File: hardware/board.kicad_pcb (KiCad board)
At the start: 2 copper layers, 146 x 40 mm, 65 parts, among them IC1 DW01A, J1 Conn_01x03_Male, J2 Conn_01x03_Male, J3 Conn_01x06, J4 Conn_01x06_Female, J5 Conn_01x06, J6 Conn_01x04, J7 Conn_01x02, P1 USB_C_Plug_USB2.0, Q1 AO3400A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

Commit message: PCB routed
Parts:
- added D10: LED, LED_SMD:LED_0805_2012Metric_Pad1.15x1.40mm_HandSolder, F.Cu at (171.2, 82.8)
- added J8: Conn_01x04, Board:Wire-Pad-01x04, B.Cu at (150.5, 90.8)
- added R23: 1k, Resistor_SMD:R_0805_2012Metric_Pad1.20x1.40mm_HandSolder, F.Cu at (171.3, 87.5)
- added R24: 100R, Resistor_SMD:R_0805_2012Metric_Pad1.20x1.40mm_HandSolder, F.Cu at (155.3, 84.9)
- added R25: 1k, Resistor_SMD:R_0805_2012Metric_Pad1.20x1.40mm_HandSolder, F.Cu at (155.2, 82.0)
- added R26: 1k, Resistor_SMD:R_0805_2012Metric_Pad1.20x1.40mm_HandSolder, F.Cu at (155.3, 87.8)
- SW3: footprint Button_Switch_SMD:SW_SPDT_PCM12 -> Board:SW_SPDT_PCM12
- moved C1 12.9 mm to (166.4, 87.7), turned to 180 degrees
- moved J4 12.5 mm to (171.0, 67.2)
- moved U1 11.3 mm to (166.4, 83.5), turned to 90 degrees
- moved C2 6.57 mm to (160.5, 87.7), turned to 180 degrees
- moved C7 5.58 mm to (170.0, 87.6), turned to 0 degrees
- moved IC1 4.69 mm to (170.0, 83.5), turned to 180 degrees
- moved D4 4.00 mm to (211.0, 80.0)
- moved D5 4.00 mm to (203.5, 77.0)
- moved J2 4.00 mm to (216.0, 74.5)
- moved Q2 4.00 mm to (211.0, 79.0)
- moved R5 4.00 mm to (211.0, 77.5)
- moved R6 4.00 mm to (207.5, 79.0)
- moved R7 4.00 mm to (207.5, 74.5)
- moved TP3 4.00 mm to (209.9, 77.0)
- moved TP4 4.00 mm to (212.5, 77.0)
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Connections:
- net /Sheet623EC3BA/AD0 renamed Net-(R10-Pad1)
- net /Sheet623EC3BA/INT renamed Net-(R12-Pad2)
- J5 pad 2: /IO34 -> /IO27
- J5 pad 3: /IO33 -> /IO26
- J5 pad 4: /IO32 -> /IO25
- J5 pad 5: /IO27 -> /IO23
- U3 pad 10: (no net) -> /IO25
- U3 pad 11: (no net) -> /IO26
- U3 pad 37: (no net) -> /IO23
- U3 pad 6: /IO34 -> /LED_B
- U3 pad 8: /IO32 -> /LED_R
- U3 pad 9: /IO33 -> /LED_G
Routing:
- net +5V: track 0.00 -> 165.1 mm
- net GND: track 0.00 -> 162.4 mm, vias 0 -> 12
- net +3V3: track 0.00 -> 150.3 mm, vias 0 -> 8
- net /SCL: track 0.00 -> 104.2 mm, vias 0 -> 1
- net /Sheet6241753E/BATT+_OUT: track 0.00 -> 102.7 mm
- net /LED_A: track 0.00 -> 96.6 mm, vias 0 -> 1
- net /LED_B: track 0.00 -> 95.2 mm, vias 0 -> 2
- net /Sheet6241753E/BATT-: track 0.00 -> 85.2 mm, vias 0 -> 1
- net /SERVO_B: track 0.00 -> 83.7 mm, vias 0 -> 1
- net /Sheet6241753E/BATT+: track 0.00 -> 79.2 mm, vias 0 -> 2
- net /SERVO_A: track 0.00 -> 69.2 mm
- net /IO0: track 0.00 -> 62.3 mm, vias 0 -> 2
- net /MOTOR_A: track 0.00 -> 58.3 mm
- net /Sheet6241753E/VBUS: track 0.00 -> 53.3 mm, vias 0 -> 4
- net /SDA: track 0.00 -> 51.6 mm, vias 0 -> 1
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- added copper zone on B.Cu, net GND
- added copper zone on F.Cu, net GND
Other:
- board size 146 x 40 mm -> 150 x 40 mm
- net class Default: clearance 0.2 -> 0.15; via_dia 0.8 -> 0.6
- rule trace_clearance: 0.2 -> 0.15

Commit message: PCB: Mounting holes for landing gear
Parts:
- added H1: MountingHole, MountingHole:MountingHole_2.2mm_M2, F.Cu at (120.0, 77.0)
- added H2: MountingHole, MountingHole:MountingHole_2.2mm_M2, F.Cu at (198.0, 77.0)

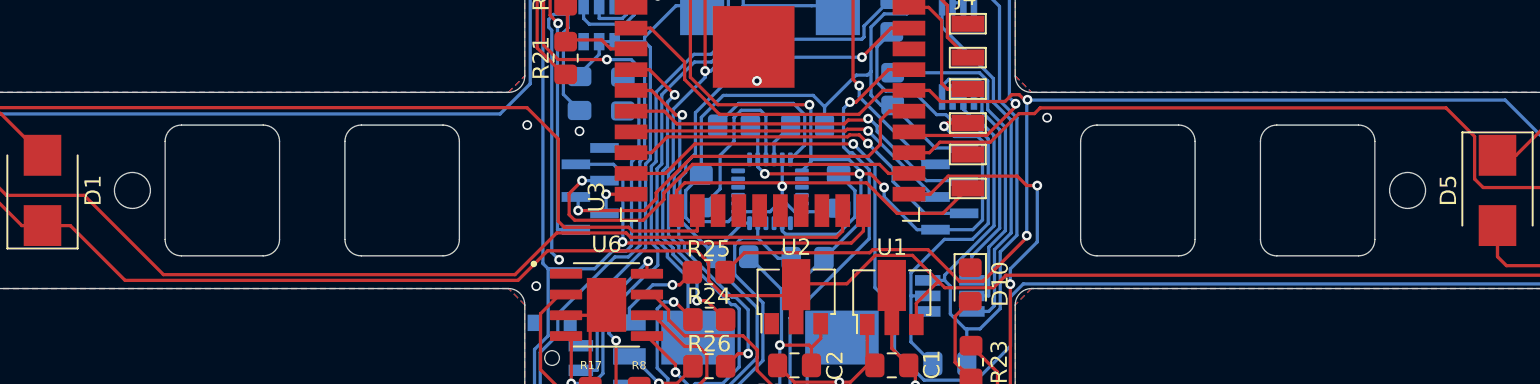
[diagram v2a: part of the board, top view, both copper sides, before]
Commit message: PCB: Holes for LiPo battery zip tie added
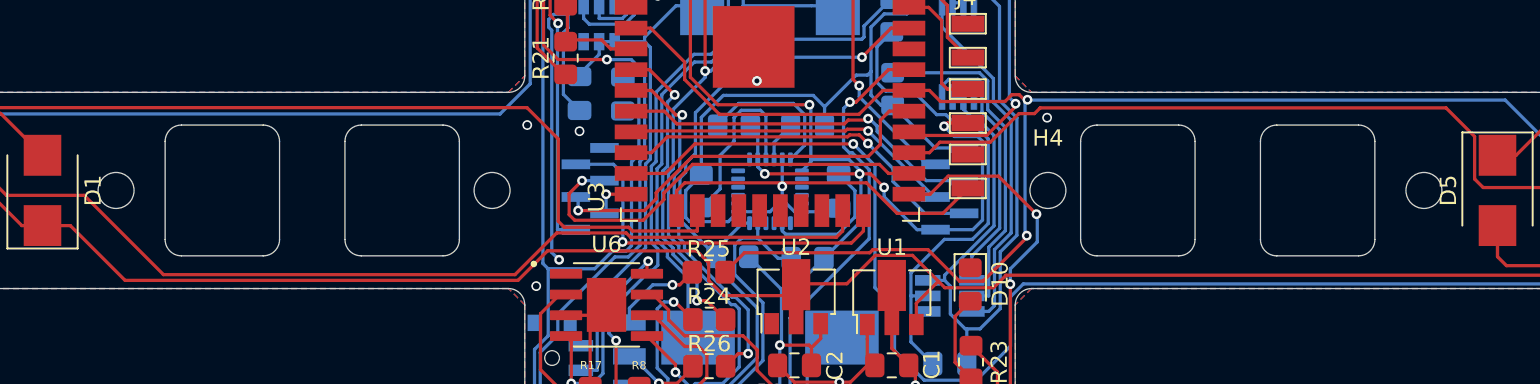
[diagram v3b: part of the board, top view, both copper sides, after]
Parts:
- added H3: MountingHole, MountingHole:MountingHole_2.2mm_M2, F.Cu at (142.0, 77.0)
- added H4: MountingHole, MountingHole:MountingHole_2.2mm_M2, F.Cu at (176.0, 77.0)
- moved H1 1.00 mm to (119.0, 77.0)
- moved H2 1.00 mm to (199.0, 77.0)
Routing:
- net /IO0: track 62.3 -> 61.2 mm

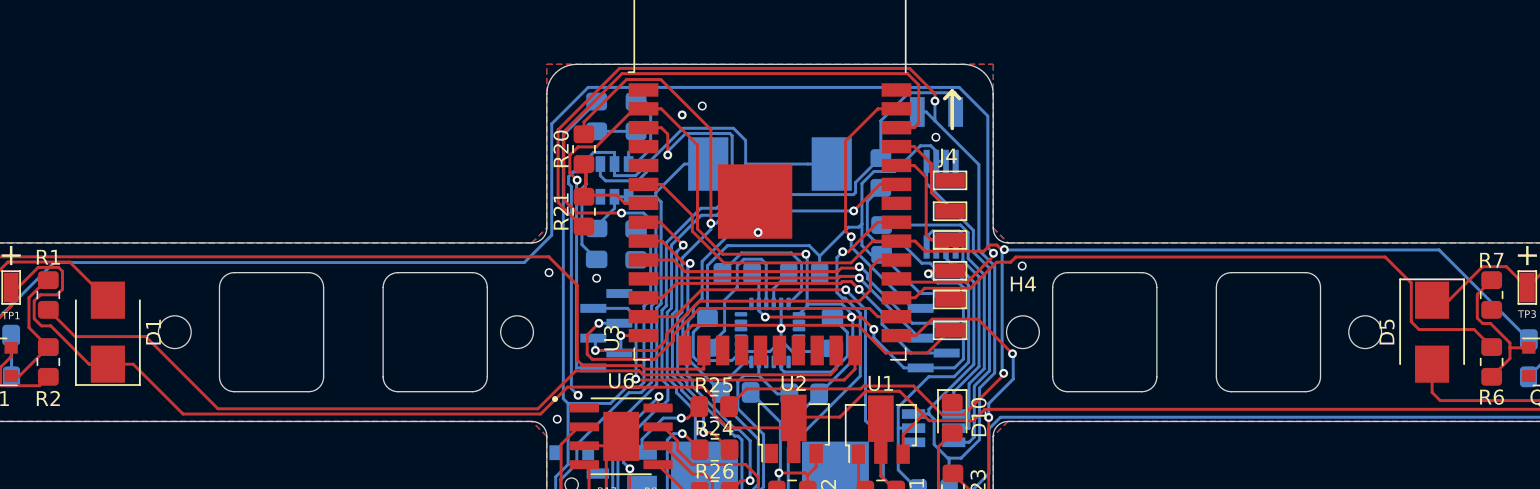
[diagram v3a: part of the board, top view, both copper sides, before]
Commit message: PCB: CE, FCC, WEEE and OSHW markings added
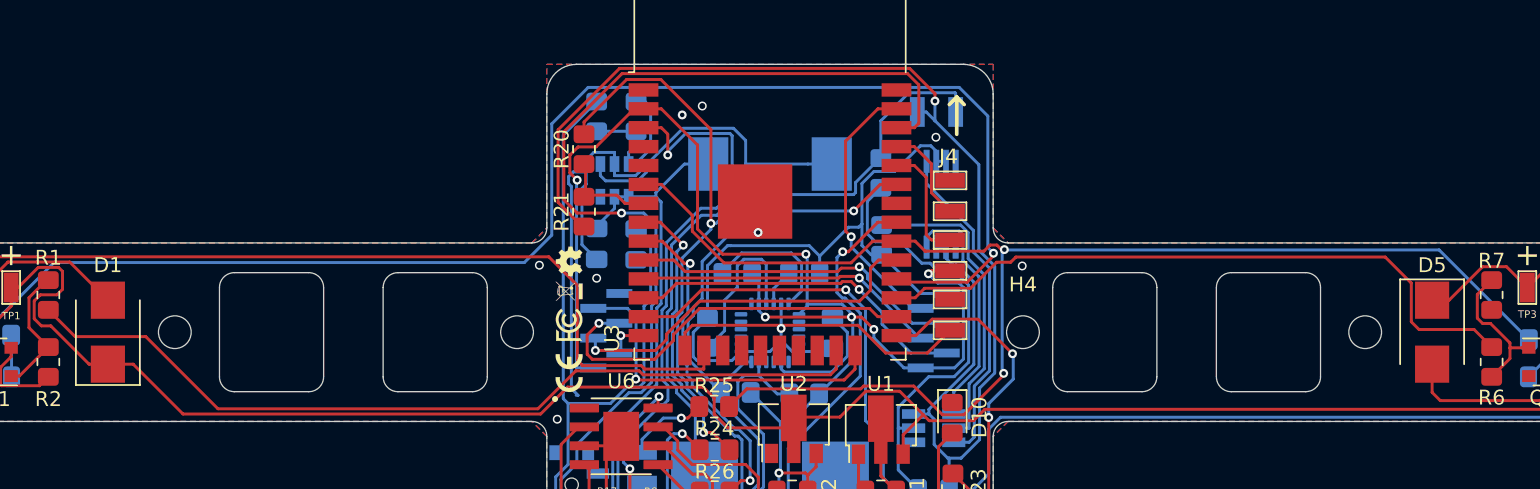
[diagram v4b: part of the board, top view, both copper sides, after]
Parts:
- added REF**: WEEE-Logo_4.2x6mm_SilkScreen, Board:WEEE-Logo-SilkScreen, F.Cu at (145.5, 74.2)
- added REF**: OSHW-Symbol_6.7x6mm_SilkScreen, Board:OSHW-Symbol-SilkScreen, F.Cu at (145.5, 72.2)
- added REF**: FCC-Logo_7.3x6mm_SilkScreen, Board:FCC-Logo-SilkScreen, F.Cu at (145.5, 76.5)
- added REF**: CE-Logo_8.5x6mm_SilkScreen, Board:CE-Logo-SilkScreen, F.Cu at (145.5, 79.8)
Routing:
- net GND: vias 12 -> 11
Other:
- board text added: "InputBlackBoxOutput"

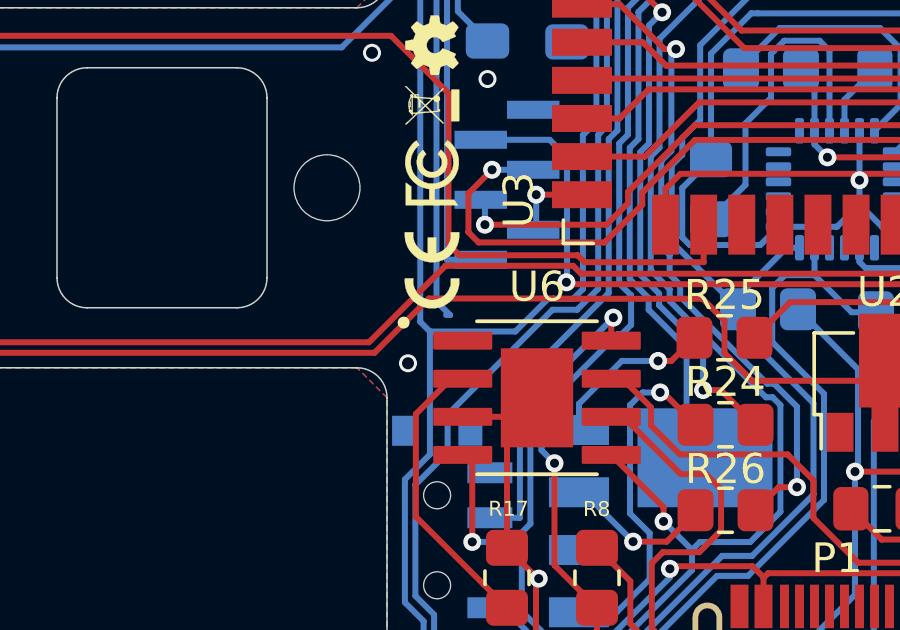
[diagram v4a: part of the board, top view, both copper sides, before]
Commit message: PCB: Fixed connection to ground plane
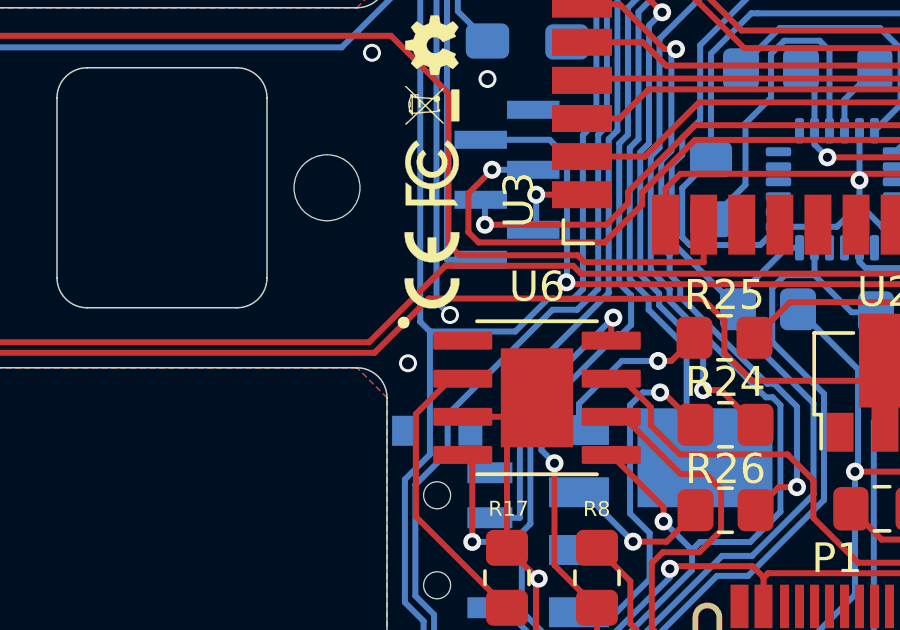
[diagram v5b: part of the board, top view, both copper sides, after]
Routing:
- net GND: vias 11 -> 12
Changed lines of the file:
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@@
     (thickness 1.6)
     (drawings 92)
-    (tracks 974)
+    (tracks 976)
     (zones 0)
     (modules 79)
@@
       (effects (font (size 1 1) (thickness 0.15)) (justify mirror))
     )
-    (fp_line (start 2.25 3.5) (end -2.25 3.5) (layer B.CrtYd) (width 0.05))
-    (fp_line (start 2.25 -3.5) (end 2.25 3.5) (layer B.CrtYd) (width 0.05))
-    (fp_line (start -2.25 -3.5) (end 2.25 -3.5) (layer B.CrtYd) (width 0.05))
-    (fp_line (start -2.25 3.5) (end -2.25 -3.5) (layer B.CrtYd) (width 0.05))
-    (fp_line (start -0.695 -2.06) (end -0.695 -3.06) (layer B.SilkS) (width 0.12))
-    (fp_line (start -0.695 -0.06) (end -0.695 -0.94) (layer B.SilkS) (width 0.12))
-    (fp_line (start -0.695 1.94) (end -0.695 1.06) (layer B.SilkS) (width 0.12))
-    (fp_line (start 0.695 -1.06) (end 0.695 -1.94) (layer B.SilkS) (width 0.12))
-    (fp_line (start 0.695 0.94) (end 0.695 0.06) (layer B.SilkS) (width 0.12))
-    (fp_line (start 0.695 3.06) (end 0.695 2.06) (layer B.SilkS) (width 0.12))
-    (fp_line (start 0.695 -3.06) (end 0.695 -3.06) (layer B.SilkS) (width 0.12))
-    (fp_line (start -0.695 3.06) (end -0.695 3.06) (layer B.SilkS) (width 0.12))
-    (fp_line (start -0.695 3.06) (end -1.69 3.06) (layer B.SilkS) (width 0.12))
-    (fp_line (start -0.695 -3.06) (end 0.695 -3.06) (layer B.SilkS) (width 0.12))
-    (fp_line (start -0.695 3.06) (end 0.695 3.06) (layer B.SilkS) (width 0.12))
-    (fp_line (start 1.25 -2.65) (end 0.635 -2.65) (layer B.Fab) (width 0.1))
-    (fp_line (start 1.25 -2.35) (end 1.25 -2.65) (layer B.Fab) (width 0.1))
-    (fp_line (start 0.635 -2.35) (end 1.25 -2.35) (layer B.Fab) (width 0.1))
-    (fp_line (start 1.25 -0.65) (end 0.635 -0.65) (layer B.Fab) (width 0.1))
-    (fp_line (start 1.25 -0.35) (end 1.25 -0.65) (layer B.Fab) (width 0.1))
-    (fp_line (start 0.635 -0.35) (end 1.25 -0.35) (layer B.Fab) (width 0.1))
-    (fp_line (start 1.25 1.35) (end 0.635 1.35) (layer B.Fab) (width 0.1))
-    (fp_line (start 1.25 1.65) (end 1.25 1.35) (layer B.Fab) (width 0.1))
-    (fp_line (start 0.635 1.65) (end 1.25 1.65) (layer B.Fab) (width 0.1))
-    (fp_line (start -1.25 -1.65) (end -0.635 -1.65) (layer B.Fab) (width 0.1))
-    (fp_line (start -1.25 -1.35) (end -1.25 -1.65) (layer B.Fab) (width 0.1))
-    (fp_line (start -0.635 -1.35) (end -1.25 -1.35) (layer B.Fab) (width 0.1))
-    (fp_line (start -1.25 0.35) (end -0.635 0.35) (layer B.Fab) (width 0.1))
-    (fp_line (start -1.25 0.65) (end -1.25 0.35) (layer B.Fab) (width 0.1))
-    (fp_line (start -0.635 0.65) (end -1.25 0.65) (layer B.Fab) (width 0.1))
-    (fp_line (start -1.25 2.35) (end -0.635 2.35) (layer B.Fab) (width 0.1))
-    (fp_line (start -1.25 2.65) (end -1.25 2.35) (layer B.Fab) (width 0.1))
-    (fp_line (start -0.635 2.65) (end -1.25 2.65) (layer B.Fab) (width 0.1))
-    (fp_line (start 0.635 3) (end 0.635 -3) (layer B.Fab) (width 0.1))
-    (fp_line (start -0.635 2.65) (end -0.285 3) (layer B.Fab) (width 0.1))
-    (fp_line (start -0.635 -3) (end -0.635 2.65) (layer B.Fab) (width 0.1))
-    (fp_line (start -0.285 3) (end 0.635 3) (layer B.Fab) (width 0.1))
     (fp_line (start 0.635 -3) (end -0.635 -3) (layer B.Fab) (width 0.1))
+    (fp_line (start -0.285 3) (end 0.635 3) (layer B.Fab) (width 0.1))
+    (fp_line (start -0.635 -3) (end -0.635 2.65) (layer B.Fab) (width 0.1))
+    (fp_line (start -0.635 2.65) (end -0.285 3) (layer B.Fab) (width 0.1))
+    (fp_line (start 0.635 3) (end 0.635 -3) (layer B.Fab) (width 0.1))
+    (fp_line (start -0.635 2.65) (end -1.25 2.65) (layer B.Fab) (width 0.1))
+    (fp_line (start -1.25 2.65) (end -1.25 2.35) (layer B.Fab) (width 0.1))
+    (fp_line (start -1.25 2.35) (end -0.635 2.35) (layer B.Fab) (width 0.1))
+    (fp_line (start -0.635 0.65) (end -1.25 0.65) (layer B.Fab) (width 0.1))
+    (fp_line (start -1.25 0.65) (end -1.25 0.35) (layer B.Fab) (width 0.1))
+    (fp_line (start -1.25 0.35) (end -0.635 0.35) (layer B.Fab) (width 0.1))
+    (fp_line (start -0.635 -1.35) (end -1.25 -1.35) (layer B.Fab) (width 0.1))
+    (fp_line (start -1.25 -1.35) (end -1.25 -1.65) (layer B.Fab) (width 0.1))
+    (fp_line (start -1.25 -1.65) (end -0.635 -1.65) (layer B.Fab) (width 0.1))
+    (fp_line (start 0.635 1.65) (end 1.25 1.65) (layer B.Fab) (width 0.1))
+    (fp_line (start 1.25 1.65) (end 1.25 1.35) (layer B.Fab) (width 0.1))
+    (fp_line (start 1.25 1.35) (end 0.635 1.35) (layer B.Fab) (width 0.1))
+    (fp_line (start 0.635 -0.35) (end 1.25 -0.35) (layer B.Fab) (width 0.1))
+    (fp_line (start 1.25 -0.35) (end 1.25 -0.65) (layer B.Fab) (width 0.1))
+    (fp_line (start 1.25 -0.65) (end 0.635 -0.65) (layer B.Fab) (width 0.1))
+    (fp_line (start 0.635 -2.35) (end 1.25 -2.35) (layer B.Fab) (width 0.1))
+    (fp_line (start 1.25 -2.35) (end 1.25 -2.65) (layer B.Fab) (width 0.1))
+    (fp_line (start 1.25 -2.65) (end 0.635 -2.65) (layer B.Fab) (width 0.1))
+    (fp_line (start -0.695 3.06) (end 0.695 3.06) (layer B.SilkS) (width 0.12))
+    (fp_line (start -0.695 -3.06) (end 0.695 -3.06) (layer B.SilkS) (width 0.12))
+    (fp_line (start -0.695 3.06) (end -1.69 3.06) (layer B.SilkS) (width 0.12))
+    (fp_line (start -0.695 3.06) (end -0.695 3.06) (layer B.SilkS) (width 0.12))
+    (fp_line (start 0.695 -3.06) (end 0.695 -3.06) (layer B.SilkS) (width 0.12))
+    (fp_line (start 0.695 3.06) (end 0.695 2.06) (layer B.SilkS) (width 0.12))
+    (fp_line (start 0.695 0.94) (end 0.695 0.06) (layer B.SilkS) (width 0.12))
+    (fp_line (start 0.695 -1.06) (end 0.695 -1.94) (layer B.SilkS) (width 0.12))
+    (fp_line (start -0.695 1.94) (end -0.695 1.06) (layer B.SilkS) (width 0.12))
+    (fp_line (start -0.695 -0.06) (end -0.695 -0.94) (layer B.SilkS) (width 0.12))
+    (fp_line (start -0.695 -2.06) (end -0.695 -3.06) (layer B.SilkS) (width 0.12))
+    (fp_line (start -2.25 3.5) (end -2.25 -3.5) (layer B.CrtYd) (width 0.05))
+    (fp_line (start -2.25 -3.5) (end 2.25 -3.5) (layer B.CrtYd) (width 0.05))
+    (fp_line (start 2.25 -3.5) (end 2.25 3.5) (layer B.CrtYd) (width 0.05))
+    (fp_line (start 2.25 3.5) (end -2.25 3.5) (layer B.CrtYd) (width 0.05))
     (fp_text user %R (at 0 0 -90) (layer B.Fab)
       (effects (font (size 1 1) (thickness 0.15)) (justify mirror))
     )
-    (pad 6 smd rect (at 0.875 -2.5) (size 1.75 0.6) (layers B.Cu B.Paste B.Mask)
-      (net 1 GND))
-    (pad 4 smd rect (at 0.875 -0.5) (size 1.75 0.6) (layers B.Cu B.Paste B.Mask)
-      (net 50 /IO25))
-    (pad 2 smd rect (at 0.875 1.5) (size 1.75 0.6) (layers B.Cu B.Paste B.Mask)
-      (net 44 /IO27))
-    (pad 5 smd rect (at -0.875 -1.5) (size 1.75 0.6) (layers B.Cu B.Paste B.Mask)
-      (net 51 /IO23))
-    (pad 3 smd rect (at -0.875 0.5) (size 1.75 0.6) (layers B.Cu B.Paste B.Mask)
-      (net 52 /IO26))
     (pad 1 smd rect (at -0.875 2.5) (size 1.75 0.6) (layers B.Cu B.Paste B.Mask)
       (net 3 +3V3))
+    (pad 3 smd rect (at -0.875 0.5) (size 1.75 0.6) (layers B.Cu B.Paste B.Mask)
+      (net 52 /IO26))
+    (pad 5 smd rect (at -0.875 -1.5) (size 1.75 0.6) (layers B.Cu B.Paste B.Mask)
+      (net 51 /IO23))
+    (pad 2 smd rect (at 0.875 1.5) (size 1.75 0.6) (layers B.Cu B.Paste B.Mask)
+      (net 44 /IO27))
+    (pad 4 smd rect (at 0.875 -0.5) (size 1.75 0.6) (layers B.Cu B.Paste B.Mask)
+      (net 50 /IO25))
+    (pad 6 smd rect (at 0.875 -2.5) (size 1.75 0.6) (layers B.Cu B.Paste B.Mask)
+      (net 1 GND))
     (model ${KISYS3DMOD}/Connector_PinHeader_1.00mm.3dshapes/PinHeader_1x06_P1.00mm_Vertical_SMD_Pin1Left.wrl
       (at (xyz 0 0 0))
@@
   (segment (start 145.4631 67.016902) (end 145.4631 66.5437) (width 0.2) (layer B.Cu) (net 1))
   (segment (start 145.64969 80.79029) (end 145.64969 67.203492) (width 0.2) (layer B.Cu) (net 1))
-  (segment (start 146.1 81.2406) (end 145.64969 80.79029) (width 0.2) (layer B.Cu) (net 1))
+  (segment (start 146.1 81.2406) (end 146.1 81.2406) (width 0.2) (layer B.Cu) (net 1))
   (via (at 144.7 82.85) (size 0.6) (drill 0.4) (layers F.Cu B.Cu) (net 1))
   (via (at 154.45 61.8) (size 0.6) (drill 0.4) (layers F.Cu B.Cu) (net 1))
@@
   (segment (start 169.575 78.4) (end 171.1 76.875) (width 0.2) (layer F.Cu) (net 1))
   (segment (start 166.769998 78.4) (end 169.575 78.4) (width 0.2) (layer F.Cu) (net 1))
+  (segment (start 146.1 81.2406) (end 145.64969 80.79029) (width 0.2) (layer B.Cu) (net 1))
+  (via (at 146.1 81.2406) (size 0.6) (drill 0.4) (layers F.Cu B.Cu) (net 1))
   (segment (start 215.5375 77.04) (end 217.1004 75.4771) (width 0.2) (layer F.Cu) (net 2))
   (segment (start 217.1004 75.4771) (end 217.1004 73.5262) (width 0.2) (layer F.Cu) (net 2))
